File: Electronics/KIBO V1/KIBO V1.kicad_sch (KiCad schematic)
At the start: 57 parts, among them M1 Motor_Servo, M10 Motor_Servo, M11 Motor_Servo, M12 Motor_Servo, M13 Motor_DC, M14 Motor_DC, M15 Motor_DC, M16 Motor_DC, M17 Fan, M18 uMotor_Servo, M19 uMotor_Servo, M2 Motor_Servo, M20 uMotor_Servo, M21 uMotor_Servo, M3 Motor_Servo, M4 Motor_Servo, M5 Motor_Servo, M6 Motor_Servo, M7 Motor_Servo, M8 Motor_Servo, M9 Motor_Servo, Q1 TIP120, Q2 TIP120, Q3 TIP120, Q4 TIP120, Q5 2N3904, SW1 SW_SPST, U1 HC-SR04, U10 UBEC, U11 uSwitch, U12 PIR, U13 uSwitch, U14 uSwitch, U15 uSwitch, U16 PWMDriver, U2 PortExt, U3 ESP32-DEVKITC, U4 GY-521, U5 DM-OLED096-636, U6 ESP32-CAM, U7 VoltConv, U8 MotorDriver, U9 MotorDriver

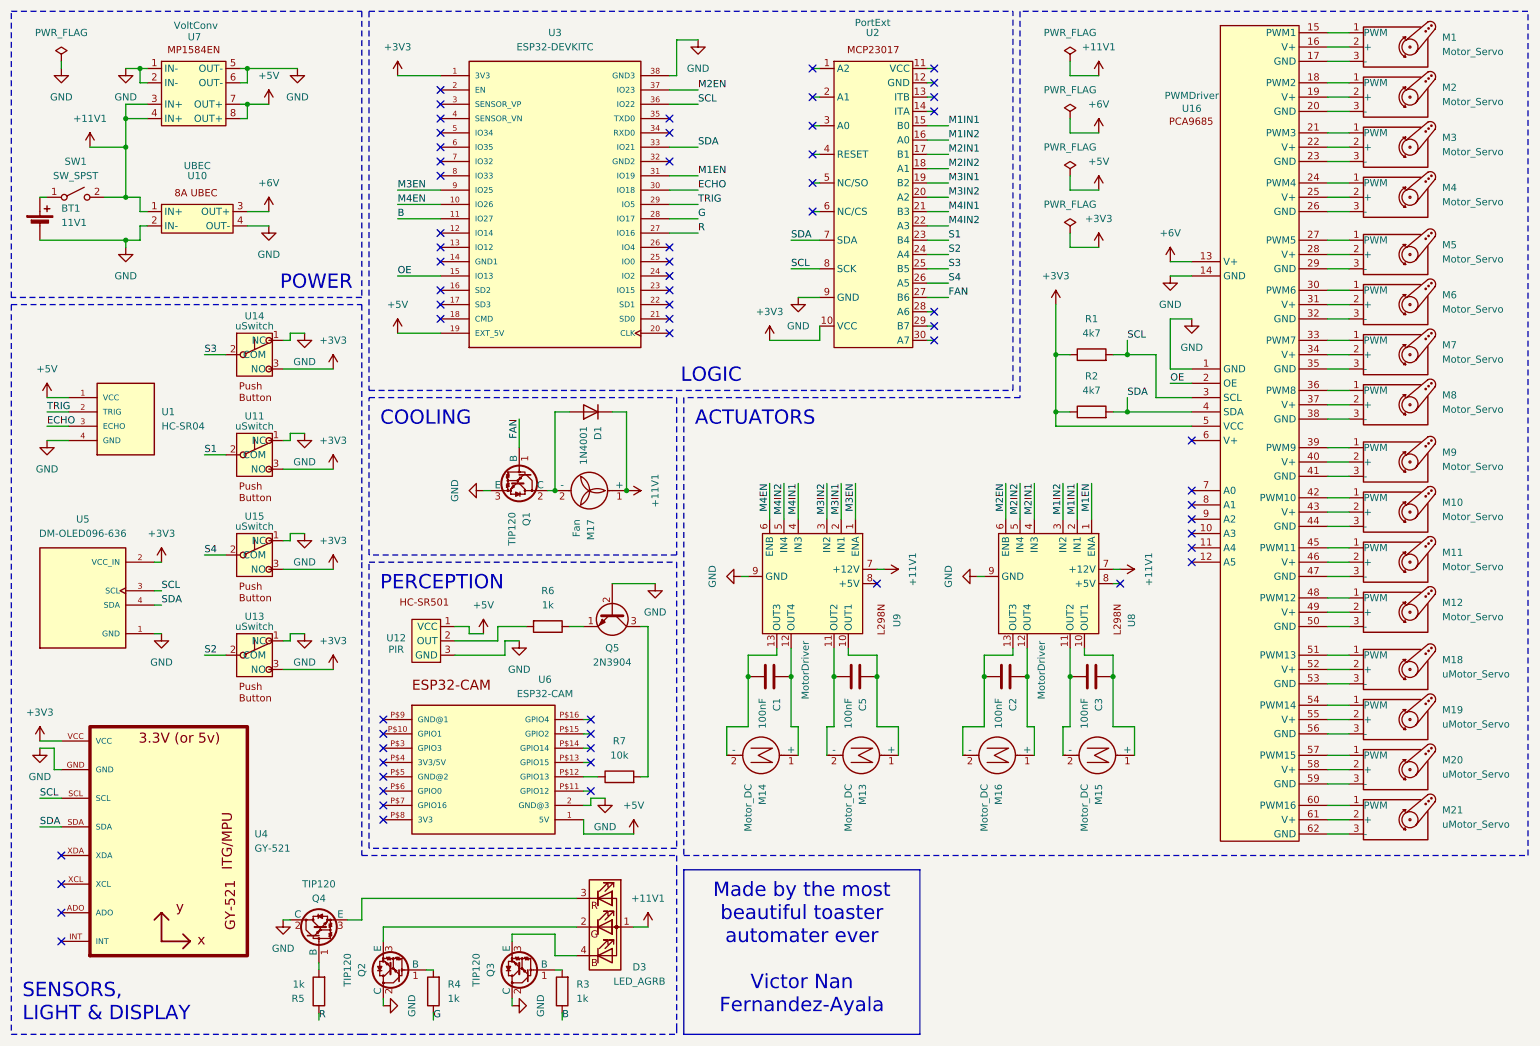
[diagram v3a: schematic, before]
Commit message: feat: added push buttons, batt measu and hc-sr04 esp32cam to schematic and footprints
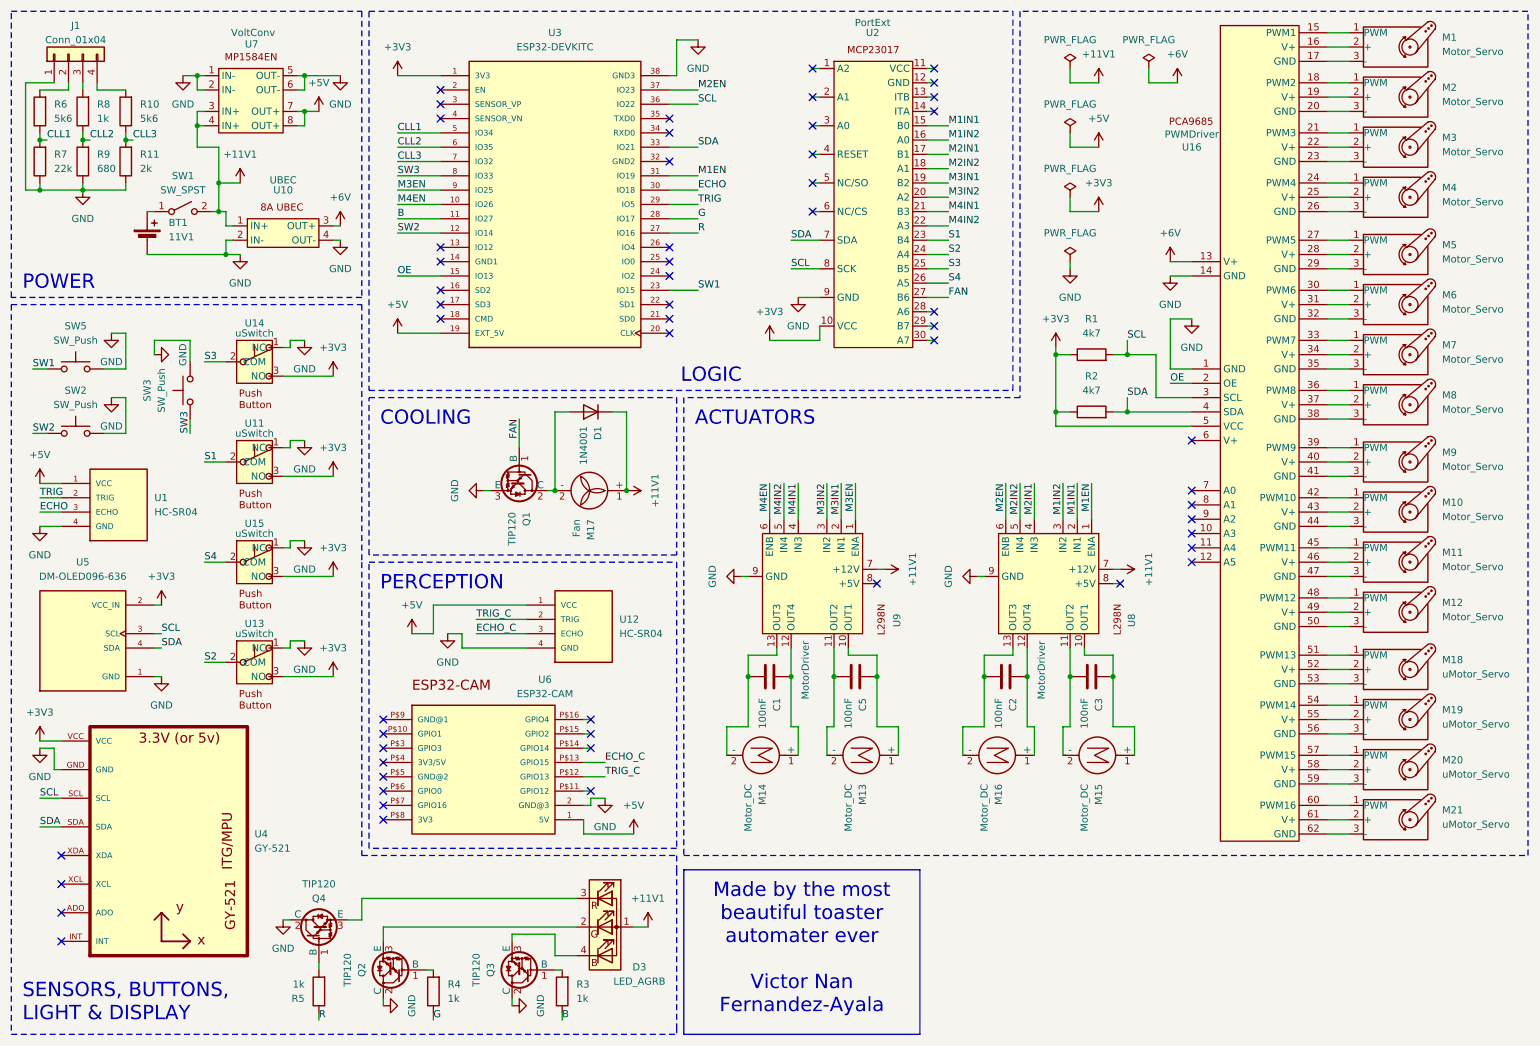
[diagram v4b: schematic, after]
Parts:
- removed Q5: 2N3904, Package_TO_SOT_THT:TO-92_Inline, symbol Transistor_BJT:2N3904
- removed U12: PIR, symbol PIRSensor_AZDelivery_HCSR501:HC-SR501
- added J1: Conn_01x04, Connector_JST:JST_EH_B4B-EH-A_1x04_P2.50mm_Vertical, symbol Connector_Generic:Conn_01x04
- added R10: 5k6, Resistor_THT:R_Axial_DIN0207_L6.3mm_D2.5mm_P7.62mm_Horizontal, symbol Device:R
- added R11: 2k, Resistor_THT:R_Axial_DIN0207_L6.3mm_D2.5mm_P7.62mm_Horizontal, symbol Device:R
- added R8: 1k, Resistor_THT:R_Axial_DIN0207_L6.3mm_D2.5mm_P7.62mm_Horizontal, symbol Device:R
- added R9: 680, Resistor_THT:R_Axial_DIN0207_L6.3mm_D2.5mm_P7.62mm_Horizontal, symbol Device:R
- added SW2, SW3, SW5: SW_Push, Button_Switch_THT:SW_PUSH_6mm, symbol Switch:SW_Push
- added U12: HC-SR04, Connector_PinHeader_2.54mm:PinHeader_1x04_P2.54mm_Vertical, symbol HC-SR04:HC-SR04
- R6: value 1k -> 5k6
- R7: value 10k -> 22k
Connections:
- net +5V: now also U12.1 (VCC)
- net GND: now also R7.1, J1.1 (Pin_1), R11.1, R9.1, SW2.2, SW3.2, SW5.2, U12.4 (GND)
- net SW2: now reaches U3.12 (IO14)
- net SW2: now also SW2.1
- net SW1: now reaches U3.23 (IO15)
- net SW1: now also SW5.1
- net CLL1: now reaches U3.5 (IO34)
- net CLL1: now also R6.1, R7.2
- net CLL2: now reaches U3.6 (IO35)
- net CLL2: now also R8.1, R9.2
- net CLL3: now reaches U3.7 (IO32)
- net CLL3: now also R10.1, R11.2
- net SW3: now reaches U3.8 (IO33)
- net SW3: now also SW3.1
- net at R6.2: now also J1.2 (Pin_2)
- net TRIG_C: now reaches U6.P$12 (GPIO13)
- net TRIG_C: now also U12.2 (TRIG); no longer R7.1
- net ECHO_C: now reaches U6.P$13 (GPIO15)
- net ECHO_C: now also U12.3 (ECHO)
- new net: J1.3 (Pin_3), R8.2
- new net: J1.4 (Pin_4), R10.2
- no-connect marks 62 -> 55
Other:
- moved on the sheet: BT1, SW1, U1, U10, U11, U13, U14, U15, U5, U7

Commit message: fix: cleaned footprint placement, text and logos
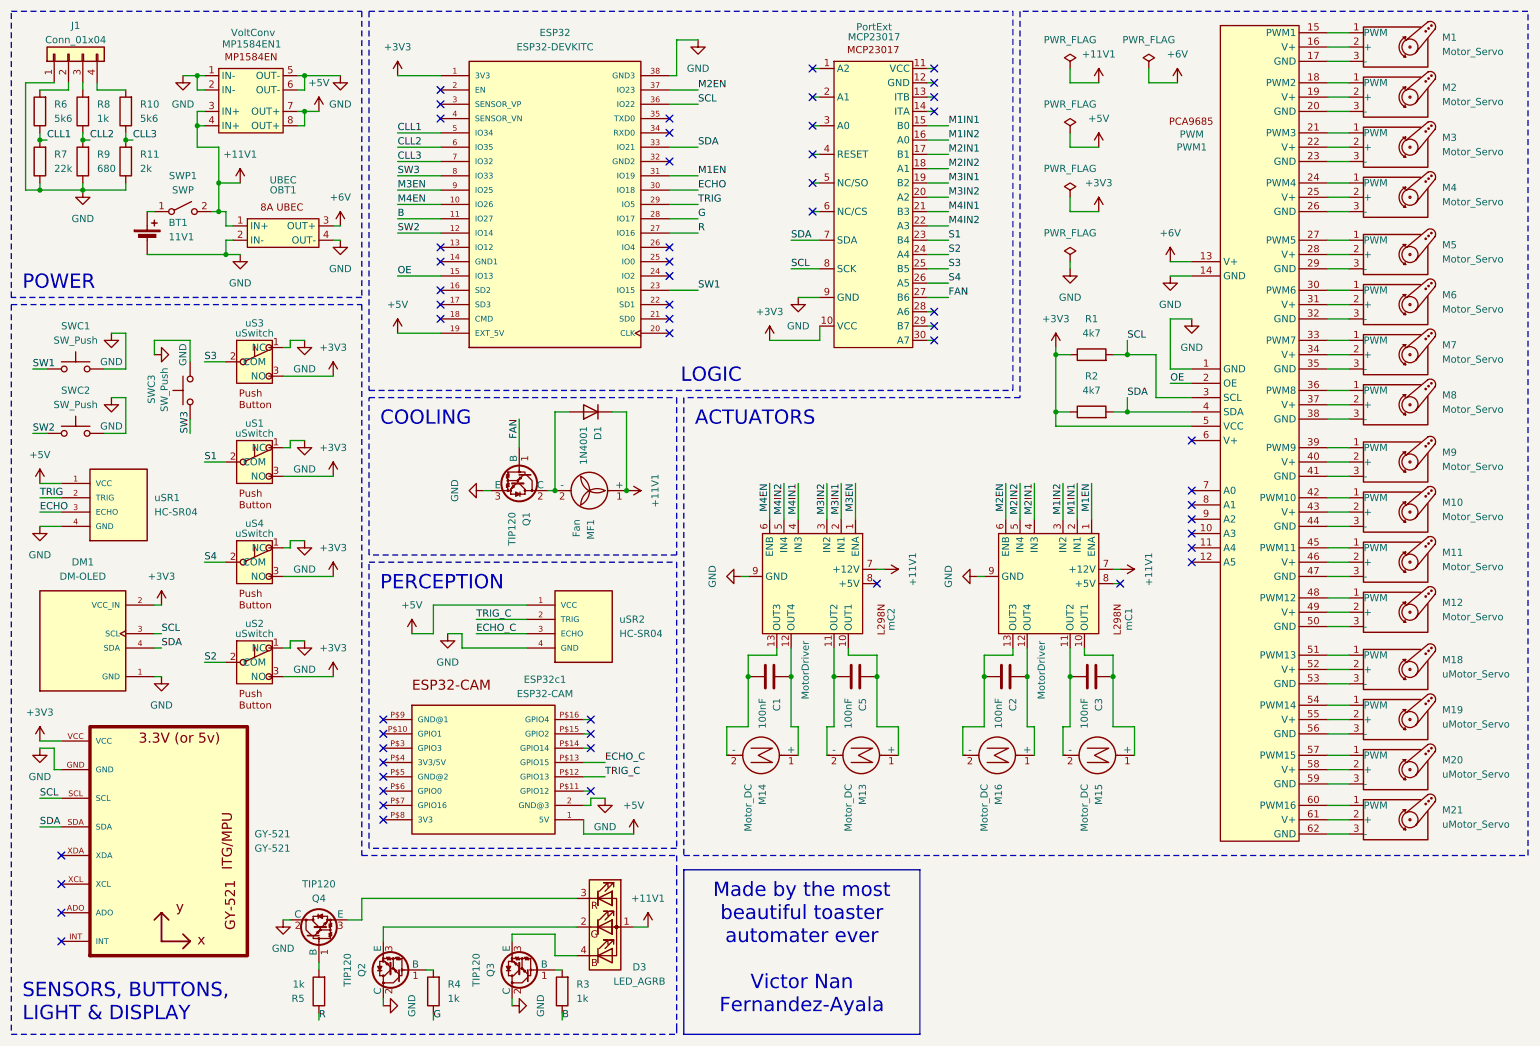
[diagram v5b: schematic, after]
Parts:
- DM1: renamed from U5; value DM-OLED096-636 -> DM-OLED
- PWM1: renamed from U16; value PWMDriver -> PWM
- SWP1: renamed from SW1; value SW_SPST -> SWP
- renumbered U3 to ESP32, U6 to ESP32c1, U4 to GY-521, U2 to MCP23017, M17 to MF1, U7 to MP1584EN1, U10 to OBT1, SW5 to SWC1, SW2 to SWC2, SW3 to SWC3, U8 to mC1, U9 to mC2, U11 to uS1, U13 to uS2, U14 to uS3, U15 to uS4, U1 to uSR1, U12 to uSR2
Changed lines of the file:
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@@
 		(dnp no)
 		(fields_autoplaced yes)
-		(property "Reference" "U1"
+		(property "Reference" "uSR1"
 			(at 39.37 100.3299 0)
 			(effects
@@
 			(project "KIBO V1"
 				(path "/2ff7a7d4-3f1a-4631-b7c7-07a10014f225"
-					(reference "U1")
+					(reference "uSR1")
 					(unit 1)
 				)
@@
 		(on_board yes)
 		(dnp no)
-		(property "Reference" "U9"
-			(at 171.196 120.904 0)
+		(property "Reference" "mC2"
+			(at 170.18 119.888 0)
 			(effects
 				(font
@@
 			(project "KIBO V1"
 				(path "/2ff7a7d4-3f1a-4631-b7c7-07a10014f225"
-					(reference "U9")
+					(reference "mC2")
 					(unit 1)
 				)
@@
 		(on_board yes)
 		(dnp no)
-		(property "Reference" "U14"
+		(property "Reference" "uS3"
 			(at 57.15 69.342 0)
 			(effects
@@
 			(project "KIBO V1"
 				(path "/2ff7a7d4-3f1a-4631-b7c7-07a10014f225"
-					(reference "U14")
+					(reference "uS3")
 					(unit 1)
 				)
@@
 		(on_board yes)
 		(dnp no)
-		(property "Reference" "U15"
+		(property "Reference" "uS4"
 			(at 57.15 104.902 0)
 			(effects
@@
 			(project "KIBO V1"
 				(path "/2ff7a7d4-3f1a-4631-b7c7-07a10014f225"
-					(reference "U15")
+					(reference "uS4")
 					(unit 1)
 				)
@@
 		(on_board yes)
 		(dnp no)
-		(property "Reference" "U13"
+		(property "Reference" "uS2"
 			(at 57.15 122.682 0)
 			(effects
@@
 			(project "KIBO V1"
 				(path "/2ff7a7d4-3f1a-4631-b7c7-07a10014f225"
-					(reference "U13")
+					(reference "uS2")
 					(unit 1)
 				)
@@
 		(on_board yes)
 		(dnp no)
-		(property "Reference" "U10"
+		(property "Reference" "OBT1"
 			(at 62.23 45.72 0)
 			(effects
@@
 			(project "KIBO V1"
 				(path "/2ff7a7d4-3f1a-4631-b7c7-07a10014f225"
-					(reference "U10")
+					(reference "OBT1")
 					(unit 1)
 				)
@@
 		(on_board yes)
 		(dnp no)
-		(property "Reference" "U11"
+		(property "Reference" "uS1"
 			(at 57.15 87.122 0)
 			(effects
@@
 			(project "KIBO V1"
 				(path "/2ff7a7d4-3f1a-4631-b7c7-07a10014f225"
-					(reference "U11")
+					(reference "uS1")
 					(unit 1)
 				)
@@
 		(dnp no)
 		(fields_autoplaced yes)
-		(property "Reference" "M17"
+		(property "Reference" "MF1"
 			(at 116.8401 104.14 0)
 			(effects
@@
 			(project "KIBO V1"
 				(path "/2ff7a7d4-3f1a-4631-b7c7-07a10014f225"
-					(reference "M17")
+					(reference "MF1")
 					(unit 1)
 				)
@@
 		(dnp no)
 		(fields_autoplaced yes)
-		(property "Reference" "U12"
+		(property "Reference" "uSR2"
 			(at 121.92 121.9199 0)
 			(effects
@@
 			(project "KIBO V1"
 				(path "/2ff7a7d4-3f1a-4631-b7c7-07a10014f225"
-					(reference "U12")
+					(reference "uSR2")
 					(unit 1)
 				)
@@
 		(dnp no)
 		(fields_autoplaced yes)
-		(property "Reference" "U3"
+		(property "Reference" "ESP32"
 			(at 110.49 17.78 0)
 			(effects
@@
 			(project "KIBO V1"
 				(path "/2ff7a7d4-3f1a-4631-b7c7-07a10014f225"
-					(reference "U3")
+					(reference "ESP32")
 					(unit 1)
 				)
@@
 		(on_board yes)
 		(dnp no)
-		(property "Reference" "U16"
+		(property "Reference" "PWM1"
 			(at 223.52 38.1 0)
 			(effects
@@
 			)
 		)
-		(property "Value" "PWMDriver"
+		(property "Value" "PWM"
 			(at 223.52 35.814 0)
 			(effects
@@
 			(project "KIBO V1"
 				(path "/2ff7a7d4-3f1a-4631-b7c7-07a10014f225"
-					(reference "U16")
+					(reference "PWM1")
 					(unit 1)
 				)
@@
 		(dnp no)
 		(fields_autoplaced yes)
-		(property "Reference" "U4"
+		(property "Reference" "GY-521"
 			(at 57.15 160.0199 0)
 			(effects
@@
 			(project "KIBO V1"
 				(path "/2ff7a7d4-3f1a-4631-b7c7-07a10014f225"
-					(reference "U4")
+					(reference "GY-521")
 					(unit 1)
 				)
@@
 		(dnp no)
 		(fields_autoplaced yes)
-		(property "Reference" "SW1"
+		(property "Reference" "SWP1"
 			(at 44.45 43.18 0)
 			(effects
@@
 			)
 		)
-		(property "Value" "SW_SPST"
+		(property "Value" "SWP"
 			(at 44.45 45.72 0)
 			(effects
@@
 			(project "KIBO V1"
 				(path "/2ff7a7d4-3f1a-4631-b7c7-07a10014f225"
-					(reference "SW1")
+					(reference "SWP1")
 					(unit 1)
 				)
@@
 		(on_board yes)
 		(dnp no)
-		(property "Reference" "U5"
+		(property "Reference" "DM1"
 			(at 26.67 111.76 0)
 			(effects
@@
 			)
 		)
-		(property "Value" "DM-OLED096-636"
+		(property "Value" "DM-OLED"
 			(at 26.67 114.3 0)
 			(effects
@@
 			(project "KIBO V1"
 				(path "/2ff7a7d4-3f1a-4631-b7c7-07a10014f225"
-					(reference "U5")
+					(reference "DM1")
 					(unit 1)
 				)
@@
 		(on_board yes)
 		(dnp no)
-		(property "Reference" "U2"
-			(at 166.878 17.78 0)
+		(property "Reference" "MCP23017"
+			(at 167.132 18.542 0)
 			(effects
 				(font
@@
 		)
 		(property "Value" "PortExt"
-			(at 166.878 16.002 0)
+			(at 167.132 16.764 0)
 			(effects
 				(font
@@
 			(project "KIBO V1"
 				(path "/2ff7a7d4-3f1a-4631-b7c7-07a10014f225"
-					(reference "U2")
+					(reference "MCP23017")
 					(unit 1)
 				)
@@
 		(dnp no)
 		(fields_autoplaced yes)
-		(property "Reference" "SW2"
+		(property "Reference" "SWC2"
 			(at 25.4 81.28 0)
 			(effects
@@
 			(project "KIBO V1"
 				(path "/2ff7a7d4-3f1a-4631-b7c7-07a10014f225"
-					(reference "SW2")
+					(reference "SWC2")
 					(unit 1)
 				)
@@
 		(on_board yes)
 		(dnp no)
-		(property "Reference" "U8"
-			(at 212.852 120.904 0)
+		(property "Reference" "mC1"
+			(at 212.344 119.888 0)
 			(effects
 				(font
@@
 			(project "KIBO V1"
 				(path "/2ff7a7d4-3f1a-4631-b7c7-07a10014f225"
-					(reference "U8")
+					(reference "mC1")
 					(unit 1)
 				)
@@
 		(on_board yes)
 		(dnp no)
-		(property "Reference" "U7"
+		(property "Reference" "MP1584EN1"
 			(at 56.642 19.812 0)
 			(effects
@@
 			(project "KIBO V1"
 				(path "/2ff7a7d4-3f1a-4631-b7c7-07a10014f225"
-					(reference "U7")
+					(reference "MP1584EN1")
 					(unit 1)
 				)
@@
 		(on_board yes)
 		(dnp no)
-		(property "Reference" "U6"
+		(property "Reference" "ESP32c1"
 			(at 108.712 132.588 0)
 			(effects
@@
 			(project "KIBO V1"
 				(path "/2ff7a7d4-3f1a-4631-b7c7-07a10014f225"
-					(reference "U6")
+					(reference "ESP32c1")
 					(unit 1)
 				)
@@
 		(dnp no)
 		(fields_autoplaced yes)
-		(property "Reference" "SW5"
+		(property "Reference" "SWC1"
 			(at 25.4 69.85 0)
 			(effects
@@
 			(project "KIBO V1"
 				(path "/2ff7a7d4-3f1a-4631-b7c7-07a10014f225"
-					(reference "SW5")
+					(reference "SWC1")
 					(unit 1)
 				)
@@
 		(on_board yes)
 		(dnp no)
-		(fields_autoplaced yes)
-		(property "Reference" "SW3"
-			(at 38.1 81.28 0)
+		(property "Reference" "SWC3"
+			(at 38.862 78.486 0)
 			(effects
 				(font
 					(size 1.27 1.27)
 				)
+				(justify right)
 			)
 		)
 		(property "Value" "SW_Push"
-			(at 40.64 81.28 0)
+			(at 41.148 77.216 0)
 			(effects
 				(font
 					(size 1.27 1.27)
 				)
+				(justify right)
 			)
 		)
@@
 			(project "KIBO V1"
 				(path "/2ff7a7d4-3f1a-4631-b7c7-07a10014f225"
-					(reference "SW3")
+					(reference "SWC3")
 					(unit 1)
 				)

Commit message: feat: finished PCB and its CAD
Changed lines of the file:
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@@
 	)
 	(junction
+		(at 38.1 49.53)
+		(diameter 0)
+		(color 0 0 0 0)
+	)
+	(junction
 		(at 46.99 25.4)
 		(diameter 0)
@@
 	)
 	(junction
+		(at 207.01 26.67)
+		(diameter 0)
+		(color 0 0 0 0)
+	)
+	(junction
 		(at 26.67 45.72)
 		(diameter 0)
@@
 	)
 	(junction
+		(at 207.01 38.1)
+		(diameter 0)
+		(color 0 0 0 0)
+	)
+	(junction
 		(at 201.93 132.08)
 		(diameter 0)
@@
 		(at 90.17 63.5)
 	)
+	(wire
+		(pts
+			(xy 34.29 49.53) (xy 38.1 49.53)
+		)
+		(stroke
+			(width 0)
+			(type default)
+		)
+	)
 	(polyline
 		(pts
@@
 	(wire
 		(pts
+			(xy 207.01 38.1) (xy 208.28 38.1)
+		)
+		(stroke
+			(width 0)
+			(type default)
+		)
+	)
+	(wire
+		(pts
 			(xy 186.69 132.08) (xy 186.69 140.97)
 		)
@@
 	(wire
 		(pts
+			(xy 207.01 26.67) (xy 208.28 26.67)
+		)
+		(stroke
+			(width 0)
+			(type default)
+		)
+	)
+	(wire
+		(pts
 			(xy 201.93 140.97) (xy 200.66 140.97)
 		)
@@
 	(wire
 		(pts
+			(xy 34.29 57.15) (xy 34.29 49.53)
+		)
+		(stroke
+			(width 0)
+			(type default)
+		)
+	)
+	(wire
+		(pts
 			(xy 177.8 72.39) (xy 176.53 72.39)
 		)
@@
 		)
 	)
+	(netclass_flag ""
+		(length 2.54)
+		(shape round)
+		(at 34.29 57.15 180)
+		(fields_autoplaced yes)
+		(effects
+			(font
+				(size 1.27 1.27)
+			)
+			(justify right bottom)
+		)
+		(property "Netclass" "+11V1"
+			(at 34.9885 59.69 0)
+			(effects
+				(font
+					(size 1.27 1.27)
+					(italic yes)
+				)
+				(justify left)
+			)
+		)
+	)
+	(netclass_flag ""
+		(length 2.54)
+		(shape round)
+		(at 208.28 38.1 180)
+		(fields_autoplaced yes)
+		(effects
+			(font
+				(size 1.27 1.27)
+			)
+			(justify right bottom)
+		)
+		(property "Netclass" "+5V"
+			(at 208.9785 40.64 0)
+			(effects
+				(font
+					(size 1.27 1.27)
+					(italic yes)
+				)
+				(justify left)
+			)
+		)
+	)
+	(netclass_flag ""
+		(length 2.54)
+		(shape round)
+		(at 208.28 26.67 180)
+		(fields_autoplaced yes)
+		(effects
+			(font
+				(size 1.27 1.27)
+			)
+			(justify right bottom)
+		)
+		(property "Netclass" "+11V1"
+			(at 208.9785 29.21 0)
+			(effects
+				(font
+					(size 1.27 1.27)
+					(italic yes)
+				)
+				(justify left)
+			)
+		)
+	)
